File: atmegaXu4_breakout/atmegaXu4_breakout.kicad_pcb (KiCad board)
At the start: 2 copper layers, 20 x 50.5 mm, 26 parts, among them J1 USB_C_Receptacle_USB2.0, J2 Header-West, J3 Header-East, J4 AVR-ISP-6, U1 ATmega32U4-MU, U2 AP2127K-3.3

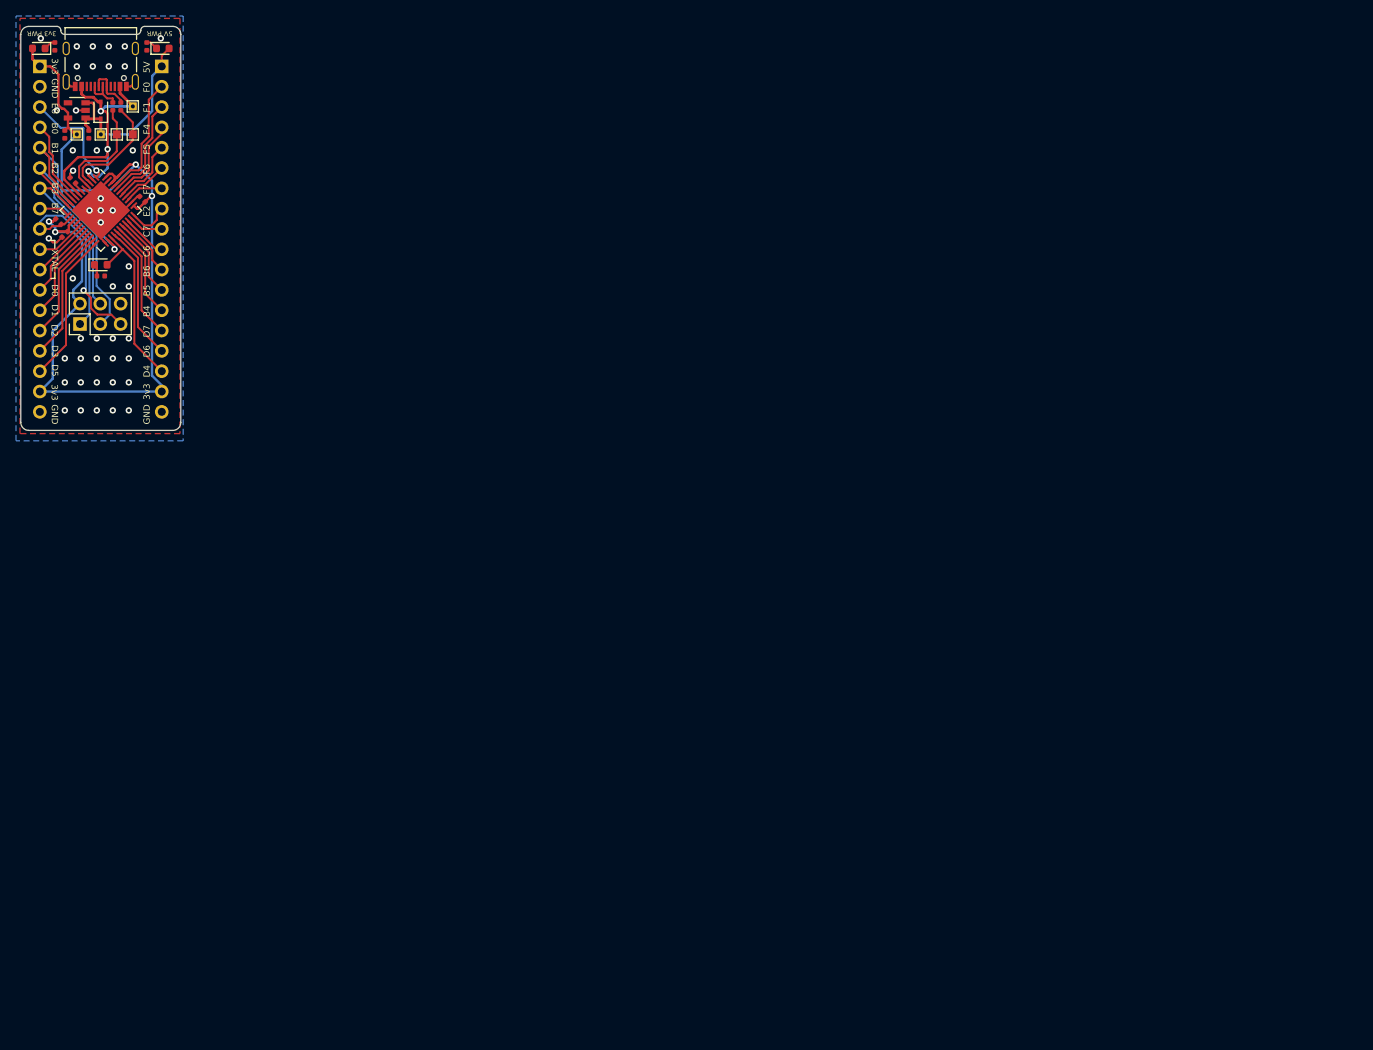
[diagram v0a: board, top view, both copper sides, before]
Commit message: Fixed missing 5.1k CC pins and cleaned up routing
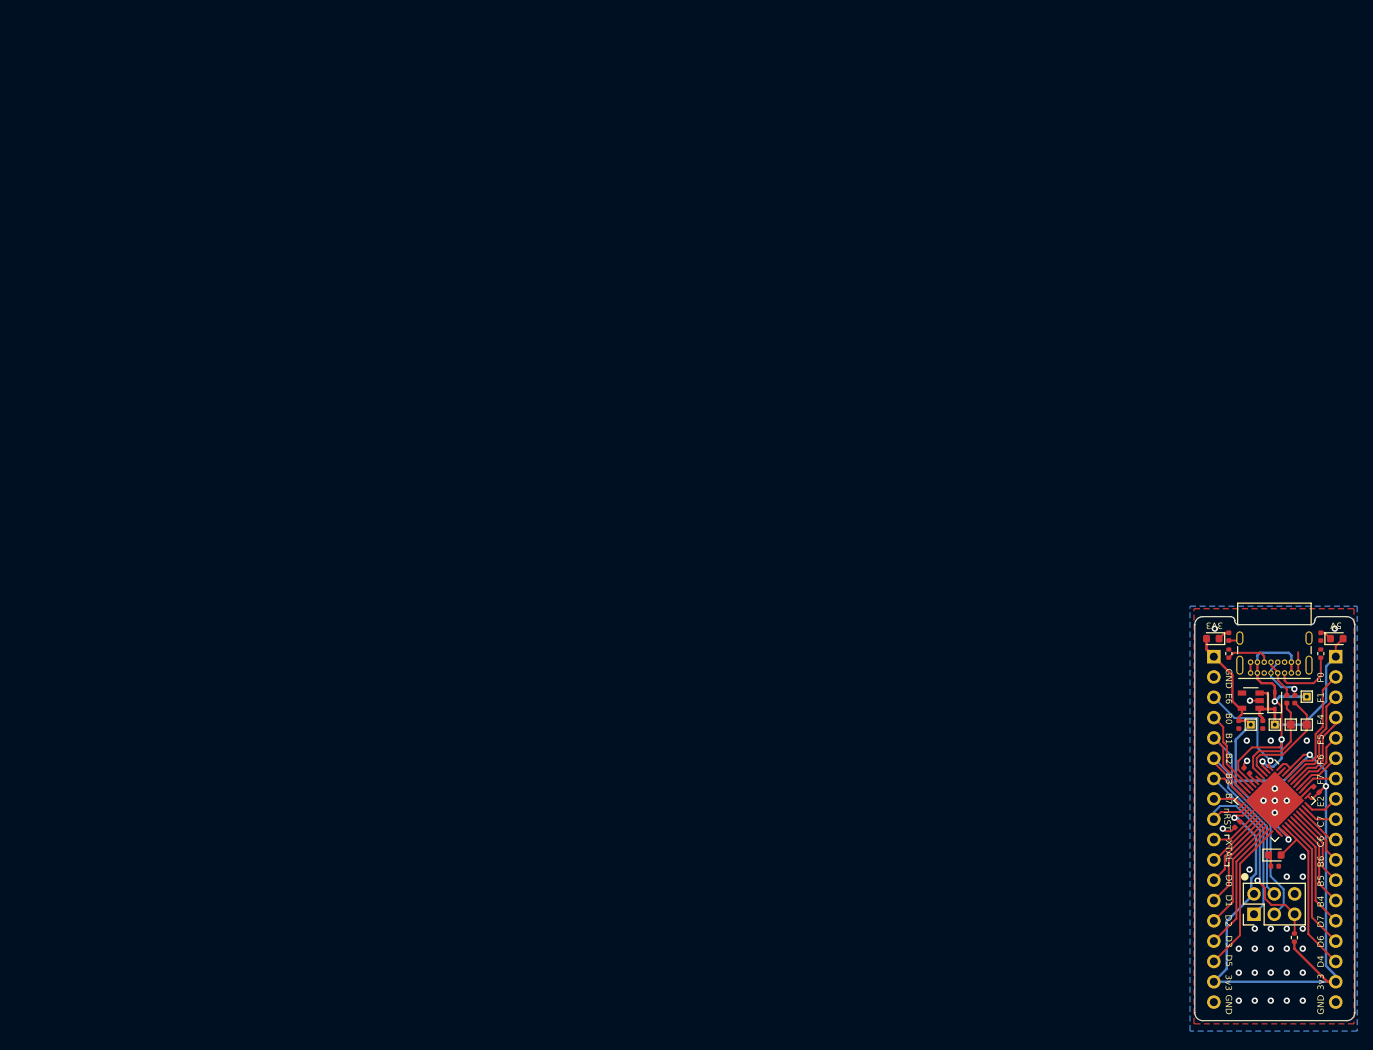
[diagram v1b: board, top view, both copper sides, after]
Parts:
- added G***: LOGO, atmega32u4_breakout:gld-logo, B.Cu at (145.9, 88.2)
- added R7: 5.1k, Resistor_SMD:R_0402_1005Metric, F.Cu at (141.0, 73.4)
- added R8: 10k, Resistor_SMD:R_0402_1005Metric, F.Cu at (149.2, 108.9)
- J1: footprint Connector_USB:USB_C_Receptacle_Palconn_UTC16-G -> Connector_USB:USB_C_Receptacle_GCT_USB4085
- R3, R4, R5: value 330 -> 470
- R6: value 10k -> 5.1k
- moved J1 167.8 mm to (149.7, 75.8)
- moved R6 166.8 mm to (152.5, 73.4), turned to -90 degrees
- moved R1 164.4 mm to (149.3, 79.1)
- moved R2 164.4 mm to (148.3, 79.1)
- moved C1 164.3 mm to (145.3, 82.3)
- moved C2 164.3 mm to (143.3, 88.0)
- moved C3 164.3 mm to (142.3, 82.3)
- moved C4 164.3 mm to (152.0, 90.4)
- moved D1 164.3 mm to (146.8, 79.3)
- moved D2 164.3 mm to (154.5, 71.5)
- moved D3 164.3 mm to (139.0, 71.5)
- moved D4 164.3 mm to (146.8, 98.6)
- moved J2 164.3 mm to (139.1, 73.8)
- moved J3 164.3 mm to (154.4, 73.8)
- moved R3 164.3 mm to (152.5, 71.3)
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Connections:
- J1 pad A8: Net-(J1-PadA8) -> unconnected-(J1-PadA8)
- J1 pad B8: Net-(J1-PadB8) -> unconnected-(J1-PadB8)
- J2 pad 9: ~RESET -> ~{RESET}
- J4 pad 5: ~RESET -> ~{RESET}
- R6 pad 1: ~RESET -> GND
- R6 pad 2: +3V3 -> Net-(J1-PadA5)
- U1 pad 13: ~RESET -> ~{RESET}
- U2 pad 4: Net-(U2-Pad4) -> unconnected-(U2-Pad4)
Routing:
- net ~{RESET}: track 0.00 -> 28.6 mm, vias 0 -> 1
- net ~RESET: track 26.2 -> 0.00 mm, vias 1 -> 0
- net Net-(J1-PadA5): track 0.00 -> 8.27 mm
- net USB_VBUS: track 35.2 -> 41.1 mm
- net Net-(J1-PadB5): track 0.00 -> 5.60 mm
- net GND: track 28.5 -> 31.0 mm, vias 45 -> 36
- net +3V3: track 131.2 -> 132.9 mm, vias 5 -> 4
- net PE2: track 5.36 -> 4.26 mm
- net Net-(J1-PadA7): track 5.94 -> 6.66 mm, vias 0 -> 1
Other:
- net class 3v3_pwr removed
- net class 5v_pwr removed
- net class Default removed
- net class USB_VBUS removed
- board text added: "3V3"
- board text added: "atmega32u4_breakout rev B"
- board text added: "nRST"
- board text removed: "3v3 PWR"
- board text removed: "5V PWR"
- board text removed: "atmegaXu4_breakout CC-BY-SA"
- board text removed: "github.com/stephendpmurphy"

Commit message: Final DRC before release
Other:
- rule pad_to_mask_clearance: 0.05 -> 0
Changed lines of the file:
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@@
   )
   (paper "A4")
+  (title_block
+    (title "atmega32u4 breakout")
+    (date "2022-12-22")
+    (rev "rev B")
+    (company "great lakes dev")
+  )
   (layers
     (0 "F.Cu" signal)
@@
       (dielectric_constraints no)
     )
-    (pad_to_mask_clearance 0.05)
+    (pad_to_mask_clearance 0)
     (pcbplotparams
       (layerselection 0x00010fc_ffffffff)
       (disableapertmacros false)
       (usegerberextensions false)
-      (usegerberattributes true)
+      (usegerberattributes false)
       (usegerberadvancedattributes true)
       (creategerberjobfile true)
@@
       (drillshape 0)
       (scaleselection 1)
-      (outputdirectory "../gerbers/")
+      (outputdirectory "../gerbers")
     )
   )
@@
     (fp_line (start 3.5 -3.5) (end 3.5 3.5) (layer "F.Fab") (width 0.1))
     (fp_line (start 3.5 3.5) (end -3.5 3.5) (layer "F.Fab") (width 0.1))
-    (pad "" smd roundrect locked (at -1.95 0.65 315) (size 1.05 1.05) (layers "F.Paste") (roundrect_rratio 0.238095))
-    (pad "" smd roundrect locked (at 1.95 1.95 315) (size 1.05 1.05) (layers "F.Paste") (roundrect_rratio 0.238095))
-    (pad "" smd roundrect locked (at -0.65 -1.95 315) (size 1.05 1.05) (layers "F.Paste") (roundrect_rratio 0.238095))
-    (pad "" smd roundrect locked (at 0.65 -0.65 315) (size 1.05 1.05) (layers "F.Paste") (roundrect_rratio 0.238095))
-    (pad "" smd roundrect locked (at 1.95 0.65 315) (size 1.05 1.05) (layers "F.Paste") (roundrect_rratio 0.238095))
-    (pad "" smd roundrect locked (at -1.95 -1.95 315) (size 1.05 1.05) (layers "F.Paste") (roundrect_rratio 0.238095))
-    (pad "" smd roundrect locked (at 0.65 0.65 315) (size 1.05 1.05) (layers "F.Paste") (roundrect_rratio 0.238095))
-    (pad "" smd roundrect locked (at -1.95 1.95 315) (size 1.05 1.05) (layers "F.Paste") (roundrect_rratio 0.238095))
-    (pad "" smd roundrect locked (at 0.65 -1.95 315) (size 1.05 1.05) (layers "F.Paste") (roundrect_rratio 0.238095))
-    (pad "" smd roundrect locked (at -0.65 -0.65 315) (size 1.05 1.05) (layers "F.Paste") (roundrect_rratio 0.238095))
-    (pad "" smd roundrect locked (at 1.95 -0.65 315) (size 1.05 1.05) (layers "F.Paste") (roundrect_rratio 0.238095))
-    (pad "" smd roundrect locked (at 0.65 1.95 315) (size 1.05 1.05) (layers "F.Paste") (roundrect_rratio 0.238095))
-    (pad "" smd roundrect locked (at -0.65 0.65 315) (size 1.05 1.05) (layers "F.Paste") (roundrect_rratio 0.238095))
-    (pad "" smd roundrect locked (at -1.95 -0.65 315) (size 1.05 1.05) (layers "F.Paste") (roundrect_rratio 0.238095))
-    (pad "" smd roundrect locked (at 1.95 -1.95 315) (size 1.05 1.05) (layers "F.Paste") (roundrect_rratio 0.238095))
-    (pad "" smd roundrect locked (at -0.65 1.95 315) (size 1.05 1.05) (layers "F.Paste") (roundrect_rratio 0.238095))
+    (pad "" smd roundrect locked (at -1.95 0.65 315) (size 1.05 1.05) (layers "F.Paste") (roundrect_rratio 0.2380952381))
+    (pad "" smd roundrect locked (at 1.95 1.95 315) (size 1.05 1.05) (layers "F.Paste") (roundrect_rratio 0.2380952381))
+    (pad "" smd roundrect locked (at -0.65 -1.95 315) (size 1.05 1.05) (layers "F.Paste") (roundrect_rratio 0.2380952381))
+    (pad "" smd roundrect locked (at 0.65 -0.65 315) (size 1.05 1.05) (layers "F.Paste") (roundrect_rratio 0.2380952381))
+    (pad "" smd roundrect locked (at 1.95 0.65 315) (size 1.05 1.05) (layers "F.Paste") (roundrect_rratio 0.2380952381))
+    (pad "" smd roundrect locked (at -1.95 -1.95 315) (size 1.05 1.05) (layers "F.Paste") (roundrect_rratio 0.2380952381))
+    (pad "" smd roundrect locked (at 0.65 0.65 315) (size 1.05 1.05) (layers "F.Paste") (roundrect_rratio 0.2380952381))
+    (pad "" smd roundrect locked (at -1.95 1.95 315) (size 1.05 1.05) (layers "F.Paste") (roundrect_rratio 0.2380952381))
+    (pad "" smd roundrect locked (at 0.65 -1.95 315) (size 1.05 1.05) (layers "F.Paste") (roundrect_rratio 0.2380952381))
+    (pad "" smd roundrect locked (at -0.65 -0.65 315) (size 1.05 1.05) (layers "F.Paste") (roundrect_rratio 0.2380952381))
+    (pad "" smd roundrect locked (at 1.95 -0.65 315) (size 1.05 1.05) (layers "F.Paste") (roundrect_rratio 0.2380952381))
+    (pad "" smd roundrect locked (at 0.65 1.95 315) (size 1.05 1.05) (layers "F.Paste") (roundrect_rratio 0.2380952381))
+    (pad "" smd roundrect locked (at -0.65 0.65 315) (size 1.05 1.05) (layers "F.Paste") (roundrect_rratio 0.2380952381))
+    (pad "" smd roundrect locked (at -1.95 -0.65 315) (size 1.05 1.05) (layers "F.Paste") (roundrect_rratio 0.2380952381))
+    (pad "" smd roundrect locked (at 1.95 -1.95 315) (size 1.05 1.05) (layers "F.Paste") (roundrect_rratio 0.2380952381))
+    (pad "" smd roundrect locked (at -0.65 1.95 315) (size 1.05 1.05) (layers "F.Paste") (roundrect_rratio 0.2380952381))
     (pad "1" smd roundrect locked (at -3.3375 -2.5 315) (size 1.075 0.25) (layers "F.Cu" "F.Paste" "F.Mask") (roundrect_rratio 0.25)
       (net 23 "PE6") (pinfunction "PE6") (pintype "bidirectional"))

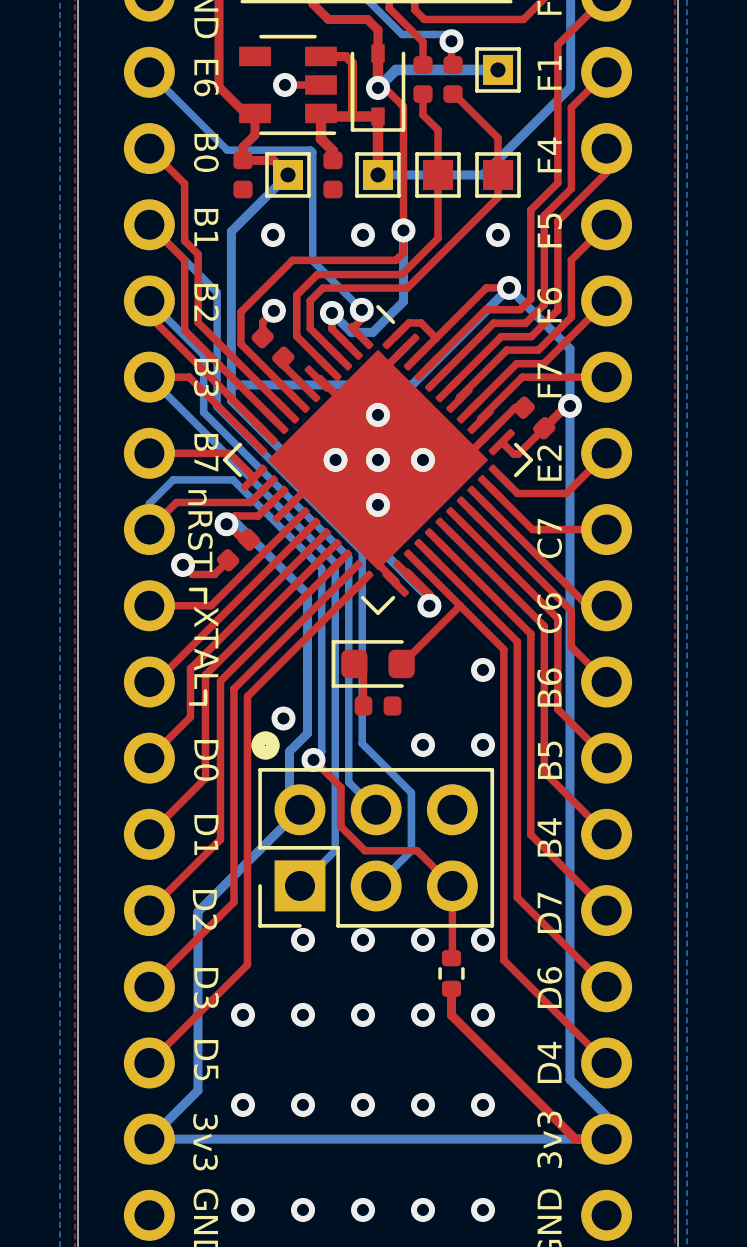
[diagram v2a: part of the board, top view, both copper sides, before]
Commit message: Added on-board 16MHz crystal
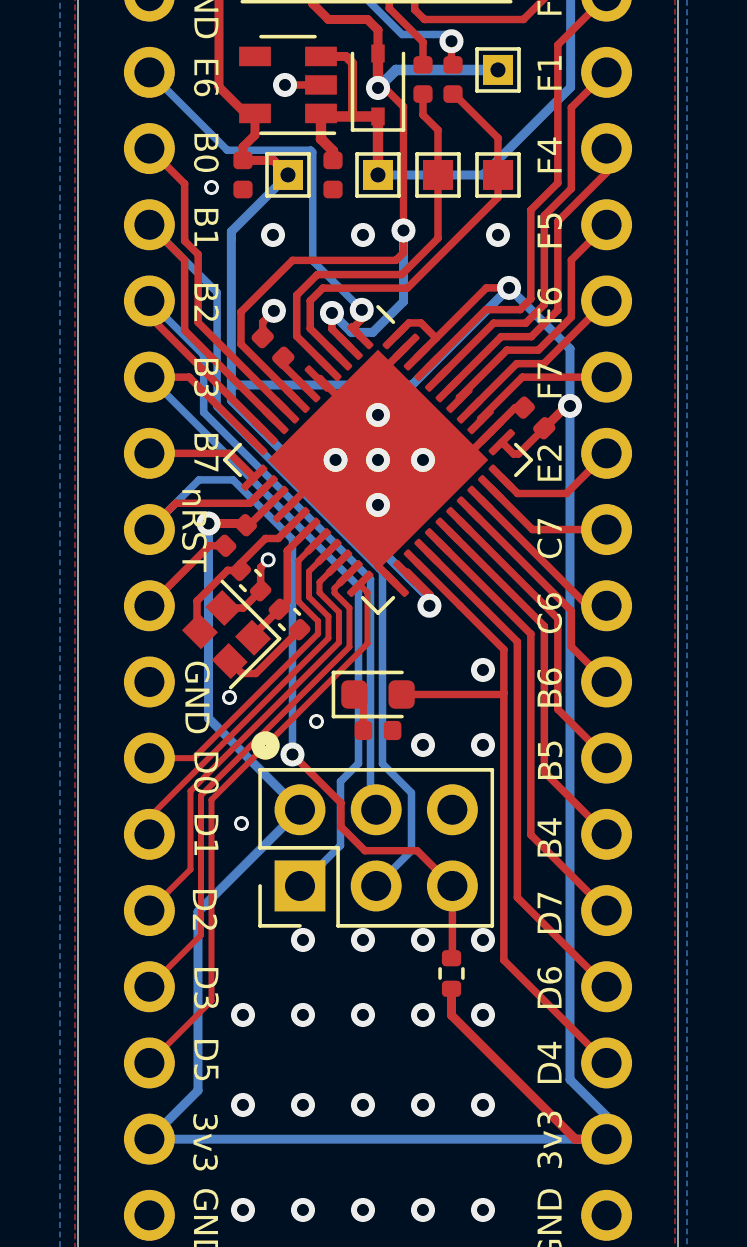
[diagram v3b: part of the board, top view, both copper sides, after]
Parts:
- added C6: 12pF, Capacitor_SMD:C_0402_1005Metric, F.Cu at (143.8, 97.1)
- added C7: 12pF, Capacitor_SMD:C_0402_1005Metric, F.Cu at (142.5, 95.8)
- added Y1: ABM11-16.000MHZ-12-N1G-T, Crystal:Crystal_SMD_2016-4Pin_2.0x1.6mm, F.Cu at (141.7, 97.6)
- moved D4 1.02 mm to (146.8, 99.6)
- moved R5 0.82 mm to (146.8, 100.8)
- moved C5 0.49 mm to (142.0, 94.3)
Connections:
- J2 pad 10: XTAL2 -> GND
- J2 pad 11: XTAL1 -> GND
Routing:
- net GND: track 31.0 -> 38.4 mm, vias 36 -> 39
- net XTAL1: track 7.35 -> 4.31 mm
- net PD0: track 9.55 -> 11.0 mm
- net +3V3: track 132.9 -> 132.2 mm
- net ~{RESET}: track 28.6 -> 27.9 mm
- net PD4: track 22.1 -> 22.7 mm
- net SPI_MISO: track 24.4 -> 25.0 mm
- net PD1: track 11.9 -> 12.4 mm
- net PD2: track 14.2 -> 14.8 mm
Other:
- board text removed: "XTAL"

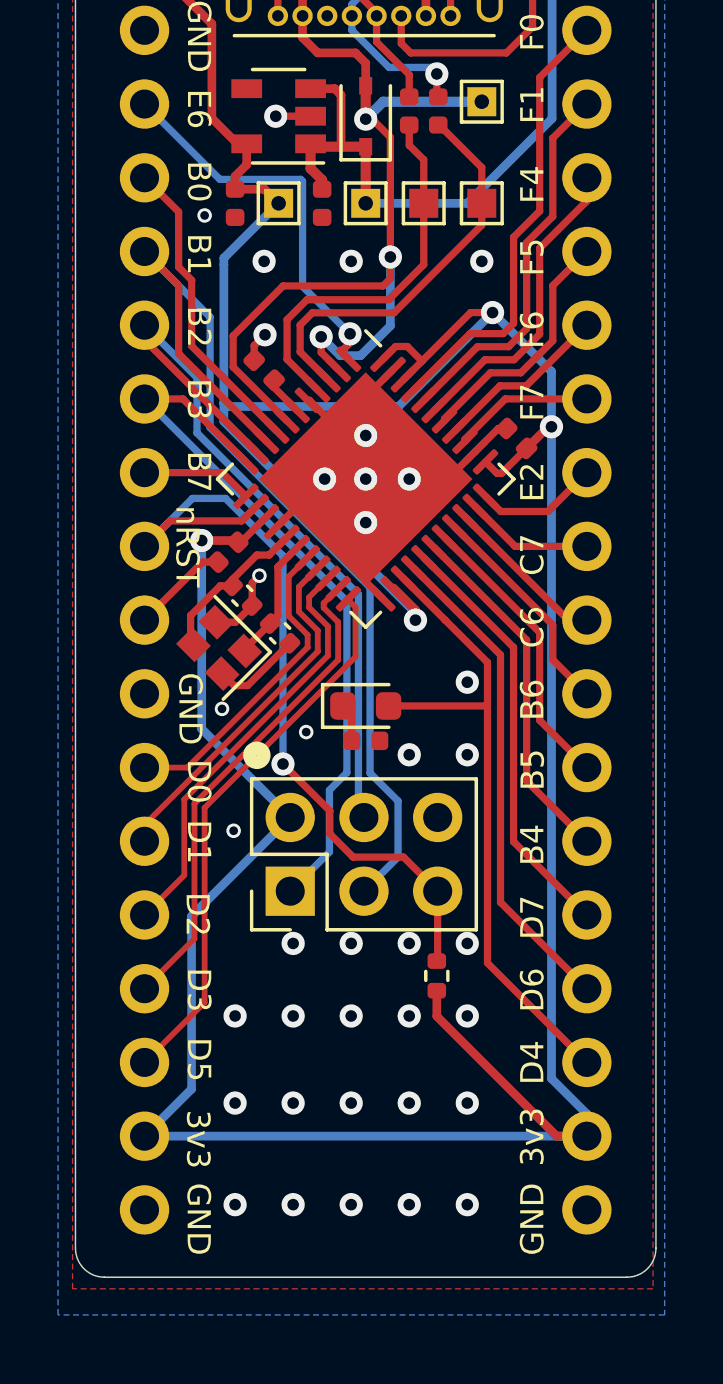
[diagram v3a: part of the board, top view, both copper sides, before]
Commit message: Added nRST and nUSR push-buttons
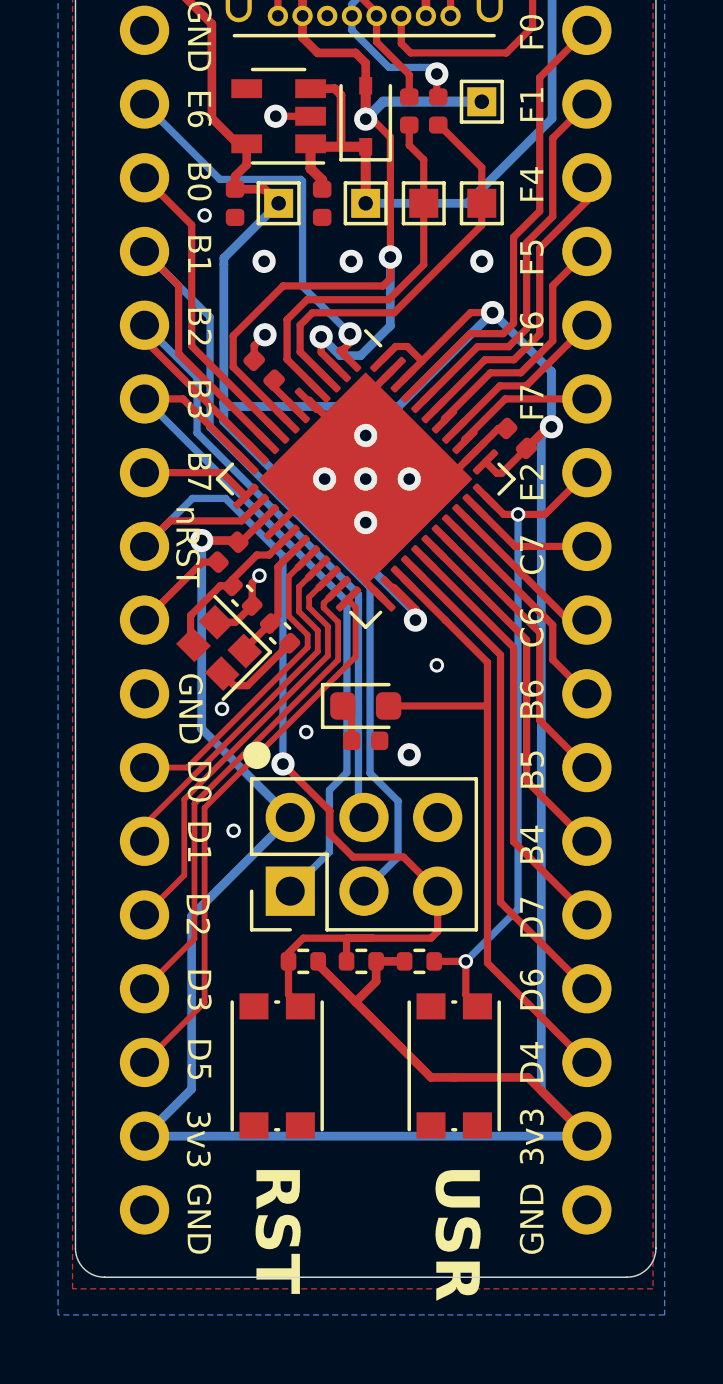
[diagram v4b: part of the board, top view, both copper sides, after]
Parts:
- added R10: 10k, Resistor_SMD:R_0402_1005Metric, F.Cu at (148.6, 108.4)
- added R9: 10k, Resistor_SMD:R_0402_1005Metric, F.Cu at (144.6, 108.4)
- added SW1: nUSR_PB, Button_Switch_SMD:SW_Push_1P1T_NO_CK_KMR2, F.Cu at (149.8, 112.0)
- added SW2: nRST_PB, Button_Switch_SMD:SW_Push_1P1T_NO_CK_KMR2, F.Cu at (143.7, 112.0)
- moved R8 2.65 mm to (146.6, 108.4), turned to 0 degrees
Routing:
- net PE2: track 4.26 -> 23.3 mm, vias 0 -> 2
- net ~{RESET}: track 27.9 -> 36.0 mm
- net +3V3: track 132.2 -> 139.2 mm
- net GND: vias 39 -> 19
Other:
- board text added: "RST"
- board text added: "USR"
